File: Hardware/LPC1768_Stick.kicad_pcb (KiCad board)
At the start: 2 copper layers, 132.1 x 50.8 mm, 86 parts, among them CON1 BARREL_JACK, CON2 USB-MINI-B, IC1 LM1117, IC2 LM1117, P1 CONN_01X40, P2 JTAG, P3 CONN_01X40, P4 USB Operation Selection, Q1 BC856, SW1 RST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

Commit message: corrected USB Drill
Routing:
- net (no net): track 7.08 -> 0.00 mm
- net GND: track 632.2 -> 639.3 mm

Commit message: Changed USB Connector
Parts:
- removed EE_LOGO: , logo:EE_LOGO(2)
- CON2: footprint Connect:USB_Micro-B -> EE:USB_Micro-B_SMD_NEW
- moved C18 4.67 mm to (209.3, 129.8)
- moved CON2 0.96 mm to (215.5, 123.6)
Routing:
- net GND: track 639.3 -> 609.9 mm, vias 17 -> 18
- net +5V: track 236.7 -> 227.5 mm
- net Net-(CON2-Pad3): track 4.29 -> 6.66 mm
- net +3.3VP: track 630.4 -> 628.8 mm
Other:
- outline, holes or cut-outs redrawn
- board text added: "BLD_D+"
- board text added: "BLD_D-"
- board text added: "HOST_D+"
- board text added: "HOST_D-"

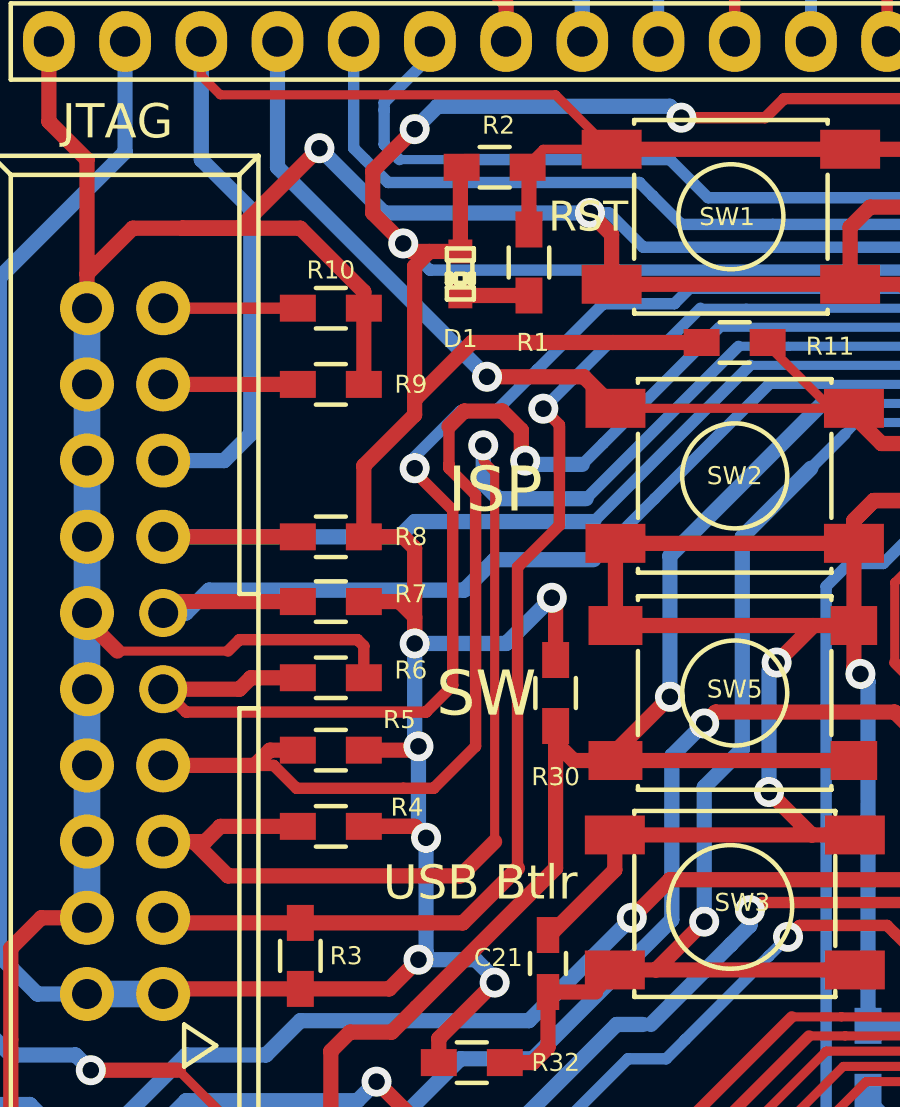
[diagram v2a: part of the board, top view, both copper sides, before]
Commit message: Modified legend fonts and generated gerber files
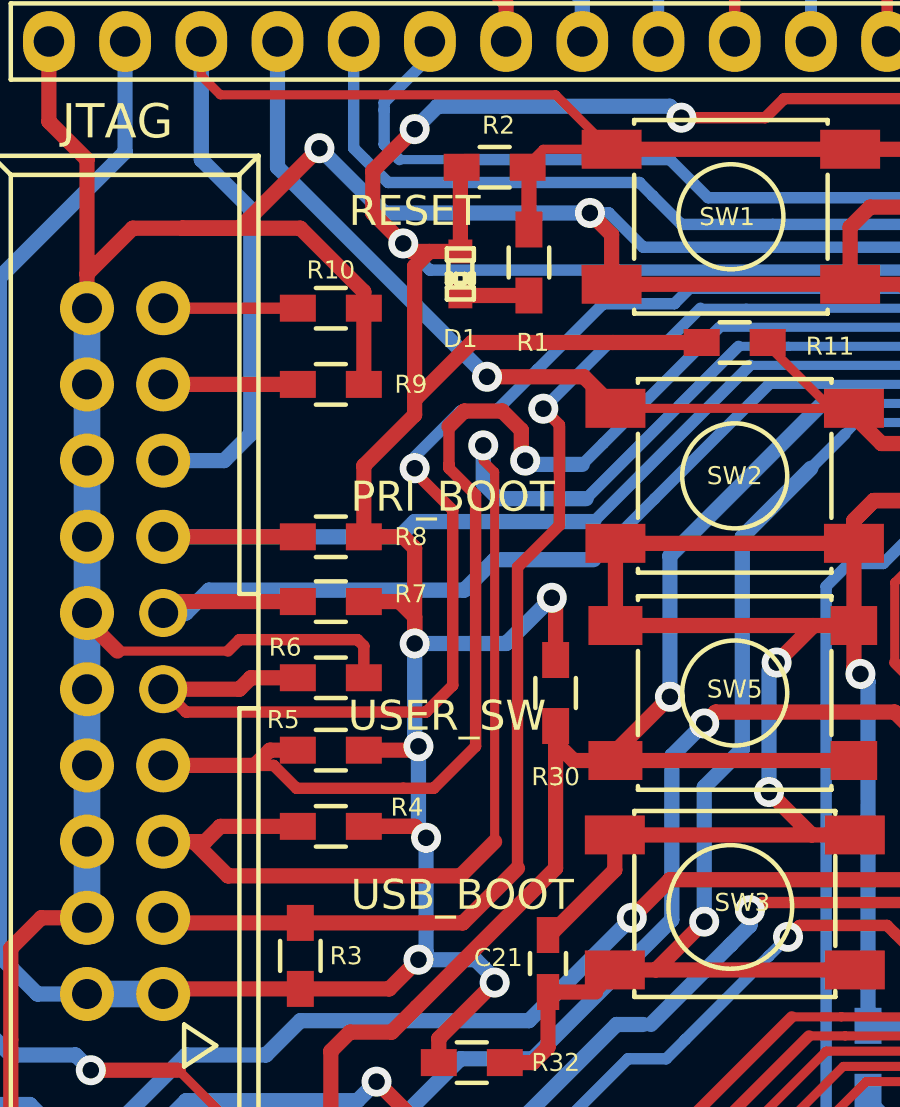
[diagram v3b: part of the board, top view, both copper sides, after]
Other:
- board text added: "PRI_BOOT"
- board text added: "RESET"
- board text added: "USB_BOOT"
- board text added: "USER_SW"
- board text added: "v1.1"
- board text removed: "ISP"
- board text removed: "RST"
- board text removed: "SW"
- board text removed: "USB Btlr"

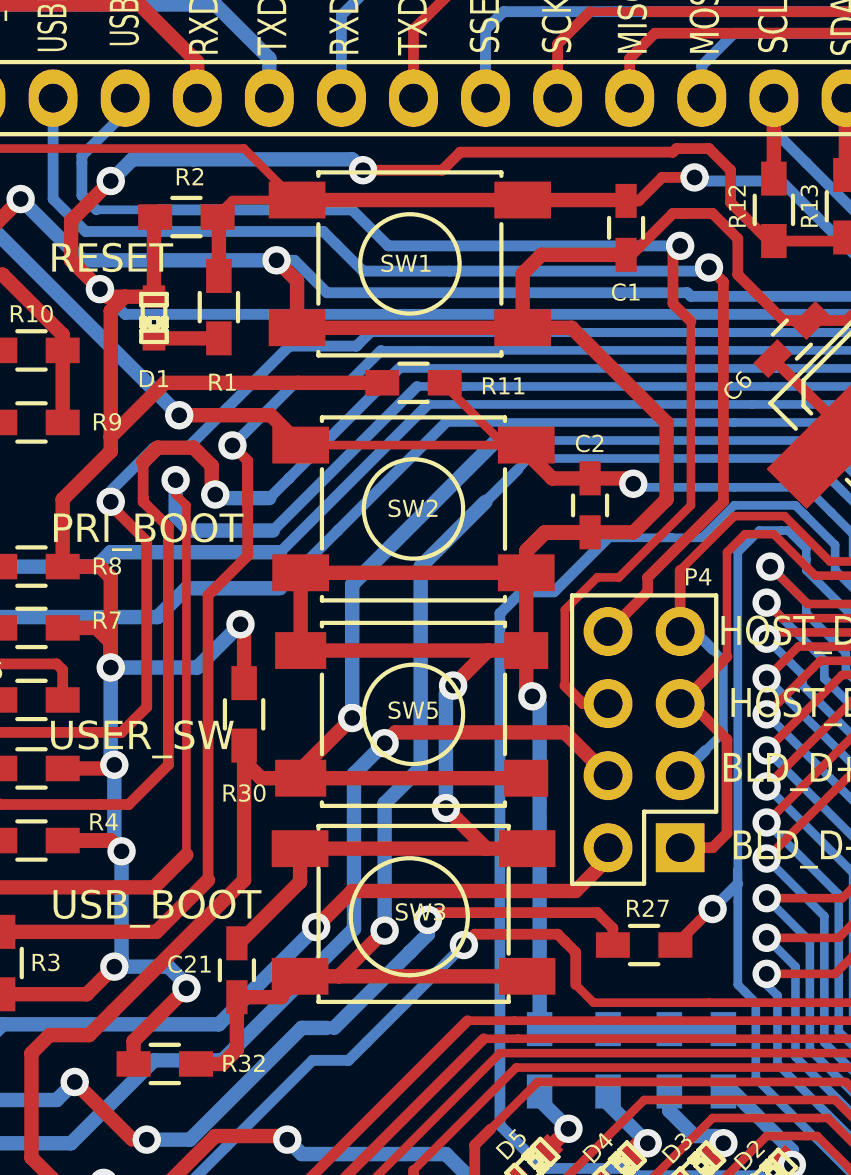
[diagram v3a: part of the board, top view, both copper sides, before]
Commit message: Changed Switches
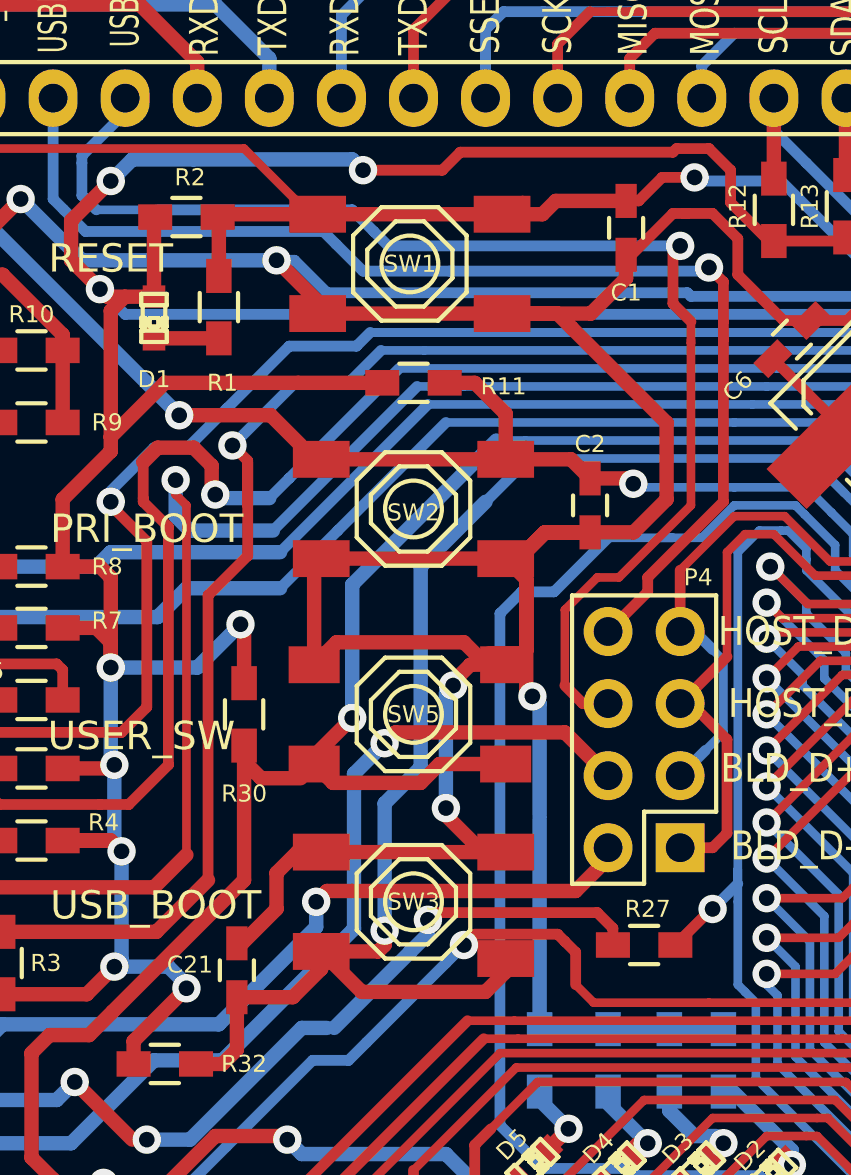
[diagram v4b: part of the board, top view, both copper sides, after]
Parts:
- moved SW3 0.28 mm to (119.4, 114.7)
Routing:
- net /~RST: track 86.9 -> 83.3 mm
- net GND: track 609.9 -> 612.4 mm
- net /u_sw_1: track 98.7 -> 97.8 mm
- net Net-(P4-Pad2): track 162.5 -> 161.8 mm
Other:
- board text added: "v1.2"
- board text removed: "v1.1"
